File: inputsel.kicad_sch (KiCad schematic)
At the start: 15 parts, among them J501 LED SW, J502 Voltage sel, Q501 2N7002, Q502 BSS84, SW501 LED Enable

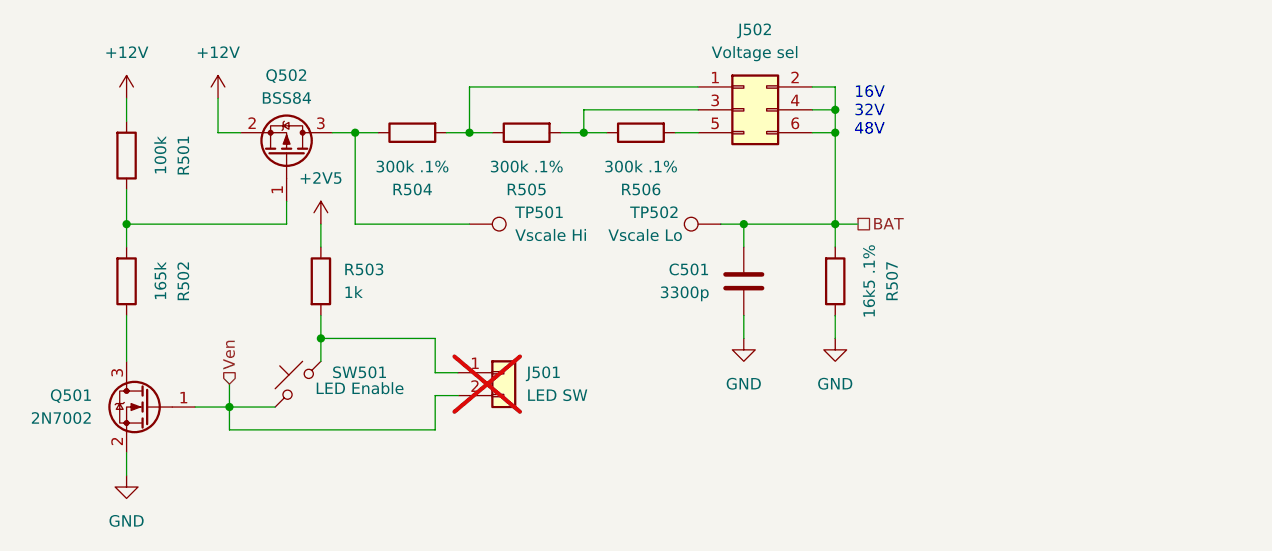
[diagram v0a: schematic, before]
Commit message: Enable external I2C programming
Signed-off-by: Benedikt Spranger <b.spranger@linutronix.de>
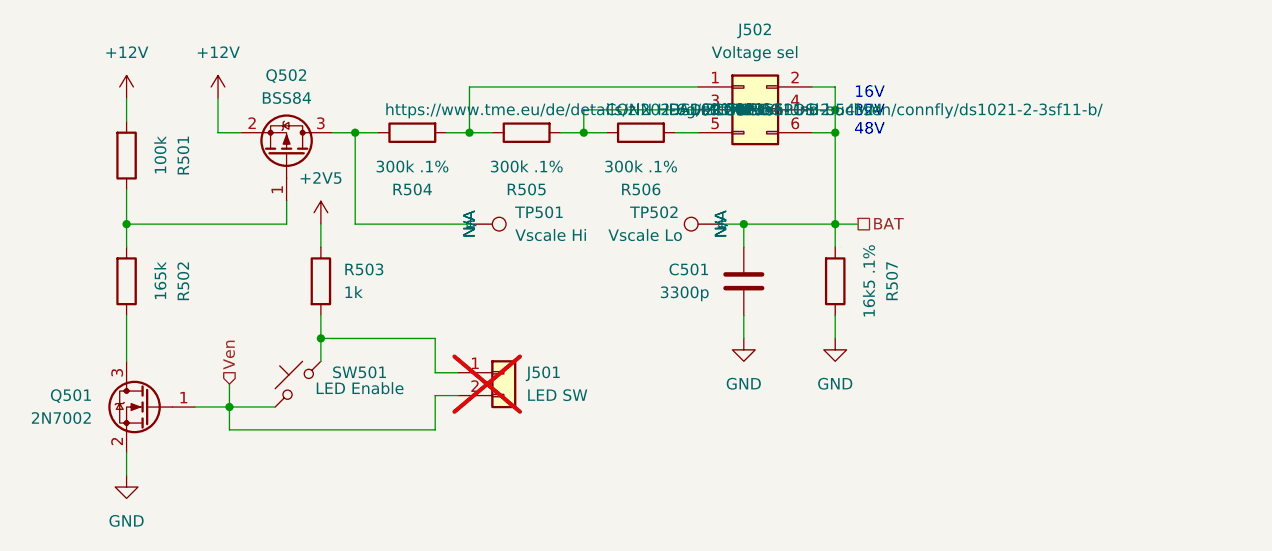
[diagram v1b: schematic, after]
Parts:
- J502: Long Description (none) -> CONN HEADER VERT 6POS 2.54MM; MF (none) -> CONFLY; MP (none) -> DS1021-2*3SF11-B; Source (none) -> TME; SupplLink (none) -> https://www.tme.eu/de/details/zl202-6g/stiftleisten-und-buc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; assemble (none) -> n; tme# (none) -> ZL202-6G
- TP501, TP502: MF (none) -> N/A; MP (none) -> N/A; Source (none) -> --; assemble (none) -> n
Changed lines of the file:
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@@
+			)
+		)
+		(property "MF" "N/A"
+			(at 154.94 77.47 0)
+			(effects
+				(font
+					(size 1.27 1.27)
+				)
+			)
+		)
+		(property "MP" "N/A"
+			(at 154.94 77.47 0)
+			(effects
+				(font
+					(size 1.27 1.27)
+				)
+			)
+		)
+		(property "Source" "--"
+			(at 154.94 77.47 0)
+			(effects
+				(font
+					(size 1.27 1.27)
+				)
+			)
+		)
+		(property "assemble" "n"
+			(at 154.94 77.47 0)
+			(effects
+				(font
+					(size 1.27 1.27)
+				)
 			)
 		)
@@
 			)
 		)
+		(property "Long Description" "CONN HEADER VERT 6POS 2.54MM"
+			(at 157.48 64.77 0)
+			(effects
+				(font
+					(size 1.27 1.27)
+				)
+			)
+		)
+		(property "MF" "CONFLY"
+			(at 157.48 64.77 0)
+			(effects
+				(font
+					(size 1.27 1.27)
+				)
+			)
+		)
+		(property "MP" "DS1021-2*3SF11-B"
+			(at 157.48 64.77 0)
+			(effects
+				(font
+					(size 1.27 1.27)
+				)
+			)
+		)
+		(property "Source" "TME"
+			(at 157.48 64.77 0)
+			(effects
+				(font
+					(size 1.27 1.27)
+				)
+			)
+		)
+		(property "SupplLink" "https://www.tme.eu/de/details/zl202-6g/stiftleisten-und-buchsen/connfly/ds1021-2-3sf11-b/"
+			(at 157.48 64.77 0)
+			(effects
+				(font
+					(size 1.27 1.27)
+				)
+			)
+		)
+		(property "assemble" "n"
+			(at 157.48 64.77 0)
+			(effects
+				(font
+					(size 1.27 1.27)
+				)
+			)
+		)
+		(property "tme#" "ZL202-6G"
+			(at 157.48 64.77 0)
+			(effects
+				(font
+					(size 1.27 1.27)
+				)
+			)
+		)
 		(pin "2"
 		)
@@
 			)
 		)
+		(property "MF" "N/A"
+			(at 127 77.47 0)
+			(effects
+				(font
+					(size 1.27 1.27)
+				)
+			)
+		)
+		(property "MP" "N/A"
+			(at 127 77.47 0)
+			(effects
+				(font
+					(size 1.27 1.27)
+				)
+			)
+		)
+		(property "Source" "--"
+			(at 127 77.47 0)
+			(effects
+				(font
+					(size 1.27 1.27)
+				)
+			)
+		)
+		(property "assemble" "n"
+			(at 127 77.47 0)
+			(effects
+				(font
+					(size 1.27 1.27)
+				)
+			)
+		)

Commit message: Available Parts
Signed-off-by: Benedikt Spranger <bene@eurovibes.org>
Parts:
- R502: MF FH (Guangdong Fenghua Advanced Tech) -> YAGEO; MP RC-02W1653FT -> RC0402FR-07165KL; SupplLink https://jlcpcb.com/partdetail/302237-RC02W1653FT/C321332 -> https://jlcpcb.com/partdetail/Yageo-RC0402FR07165KL/C327368; lcsc# C321332 -> C327368
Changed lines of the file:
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@@
 			)
 		)
-		(property "lcsc#" "C321332"
+		(property "lcsc#" "C327368"
 			(at 88.9 83.82 0)
 			(effects
@@
 			)
 		)
-		(property "SupplLink" "https://jlcpcb.com/partdetail/302237-RC02W1653FT/C321332"
+		(property "SupplLink" "https://jlcpcb.com/partdetail/Yageo-RC0402FR07165KL/C327368"
 			(at 88.9 83.82 0)
 			(effects
@@
 			)
 		)
-		(property "MF" "FH (Guangdong Fenghua Advanced Tech)"
+		(property "MF" " YAGEO"
 			(at 88.9 83.82 0)
 			(effects
@@
 			)
 		)
-		(property "MP" "RC-02W1653FT"
+		(property "MP" " RC0402FR-07165KL"
 			(at 88.9 83.82 0)
 			(effects
